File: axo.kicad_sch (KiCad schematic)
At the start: 55 parts, among them Q1 MMBT3904, Q2 MMBT3904, Q3 MMBT3904, Q4 MMBT3904, U1 74HC00, U2 74HC86, U3 74HC02, U4 LM1117-5.0

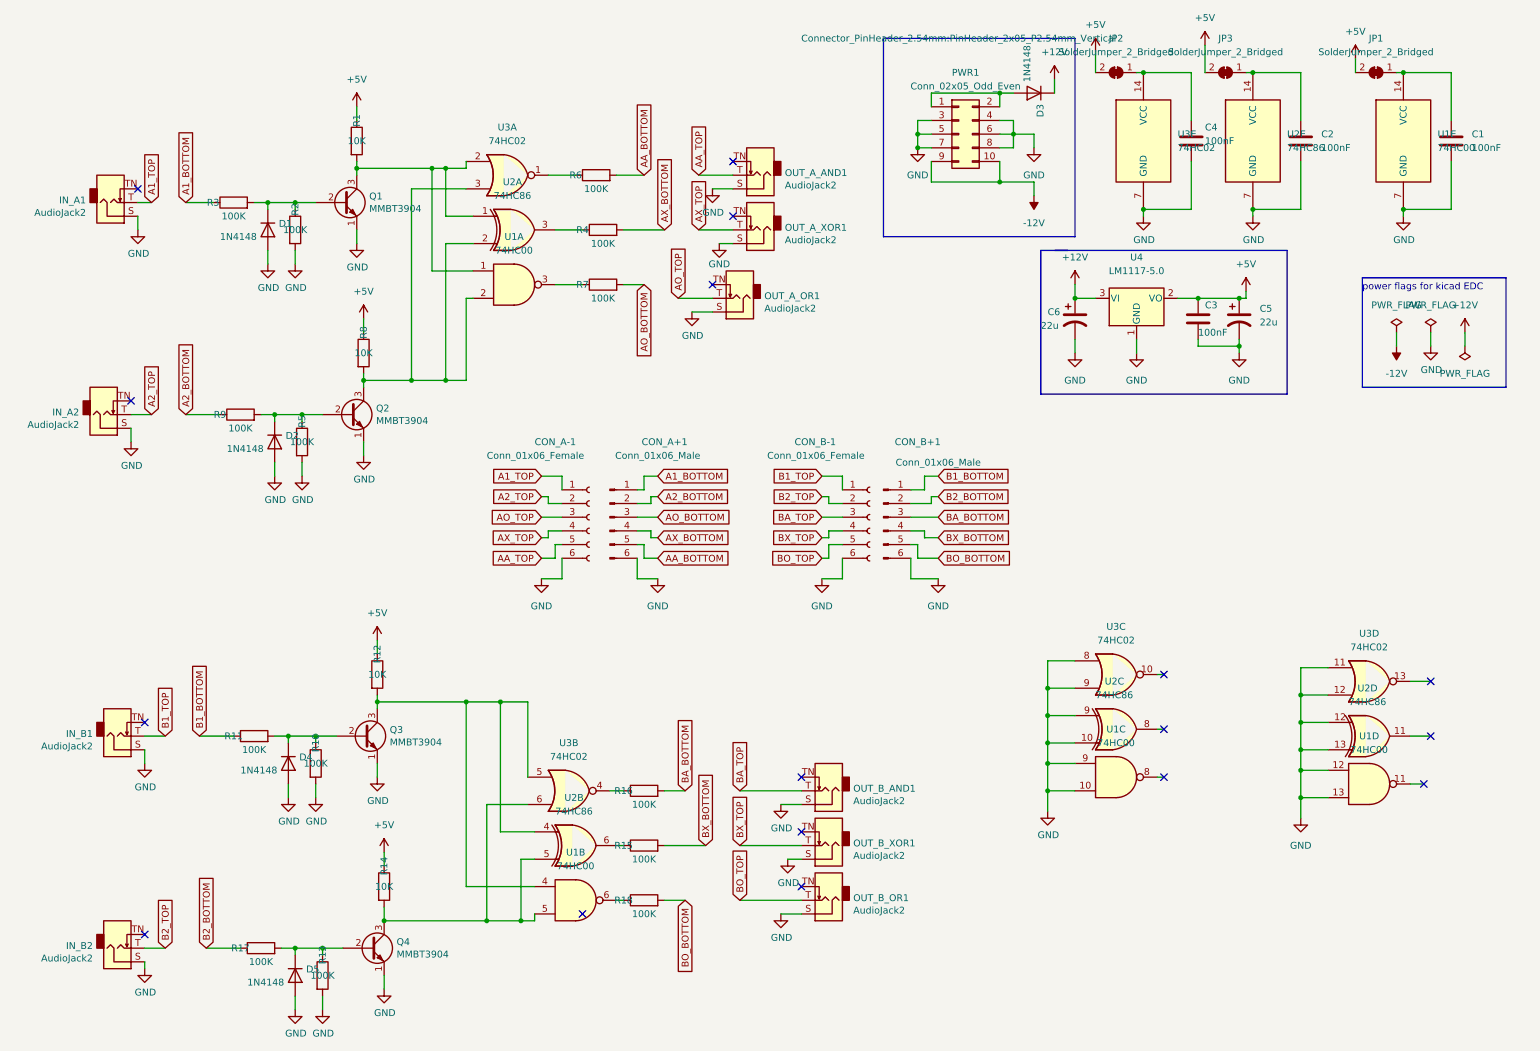
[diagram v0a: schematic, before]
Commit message: replace xor by nand/nor logic
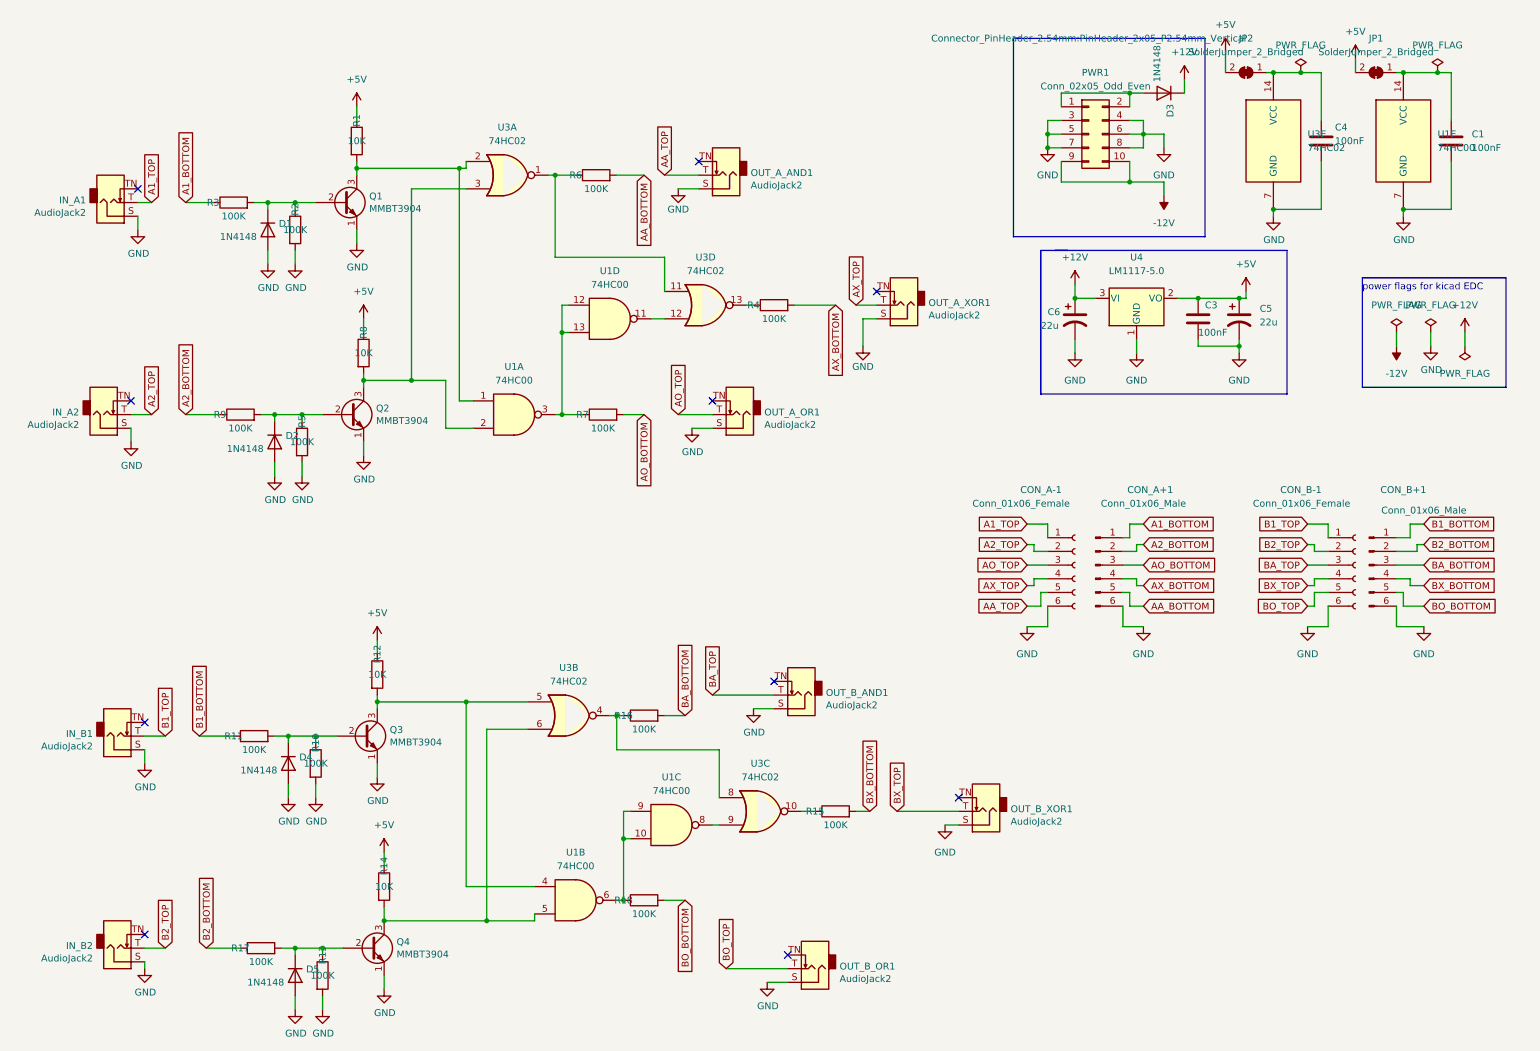
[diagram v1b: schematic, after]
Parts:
- removed C2: 100nF, Capacitor_SMD:C_0805_2012Metric, symbol Device:C
- removed JP3: SolderJumper_2_Bridged, Jumper:SolderJumper-2_P1.3mm_Bridged_Pad1.0x1.5mm, symbol Jumper:SolderJumper_2_Bridged
- removed U2: 74HC86, Package_SO:SOIC-14_3.9x8.7mm_P1.27mm, symbol 74xx:74HC86
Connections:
- net GND: no longer U1.10, U1.12, U1.13, U1.9, U3.11, U3.12, U3.8, U3.9
- net at R18.1, U1.6: now also U1.10, U1.9
- net at R15.1: now also U3.10
- net at R16.1, U3.4: now also U3.8
- net at R4.1: now also U3.13
- net at U1.11: now also U3.12
- net at R7.1, U1.3: now also U1.12, U1.13
- net at R6.1, U3.1: now also U3.11
- net at U1.8: now also U3.9
- no-connect marks 17 -> 10
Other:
- moved on the sheet: C4, CON_A+1, CON_A-1, CON_B+1, CON_B-1, D3, JP2, OUT_A_AND1, OUT_A_OR1, OUT_A_XOR1, OUT_B_AND1, OUT_B_OR1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

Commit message: add readme
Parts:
- removed Q1, Q2, Q3, Q4: MMBT3904, Package_TO_SOT_SMD:SOT-23, symbol Device:Q_NPN_EBC
- added Q1, Q2, Q3, Q4: MMBT3904, Package_TO_SOT_SMD:SOT-23, symbol Transistor_BJT:MMBT3904
- CON_A+1, CON_B+1: value Conn_01x06_Male -> Conn_01x06_Pin; symbol Connector:Conn_01x06_Male -> Connector:Conn_01x06_Pin
- CON_A-1, CON_B-1: value Conn_01x06_Female -> Conn_01x06_Socket; symbol Connector:Conn_01x06_Female -> Connector:Conn_01x06_Socket
- U4: value LM1117-5.0 -> LM1117MP-5.0; symbol Regulator_Linear:LM1117-5.0 -> Regulator_Linear:LM1117MP-5.0; LCSC C473812 -> C6187
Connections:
- net GND: now also Q1.2 (E), Q2.2 (E), Q3.2 (E), Q4.2 (E); no longer CON_A-1.6 (Pin_6), CON_B-1.6 (Pin_6), IN_A1.S, IN_A2.S, IN_B1.S, IN_B2.S, OUT_A_AND1.S, OUT_A_OR1.S, OUT_A_XOR1.S, OUT_B_AND1.S, OUT_B_OR1.S, OUT_B_XOR1.S
- net at R12.2, U1.4, U3.5: now also Q3.3 (C)
- net at R14.2, U1.5, U3.6: now also Q4.3 (C)
- net at D2.1 (K), R5.1, R9.2: now also Q2.1 (B)
- net at R8.2, U1.2, U3.3: now also Q2.3 (C)
- net at D1.1 (K), R2.1, R3.2: now also Q1.1 (B)
- net at D5.1 (K), R13.1, R17.2: now also Q4.1 (B)
- net at R1.2, U1.1, U3.2: now also Q1.3 (C)
- net at D4.1 (K), R10.1, R11.2: now also Q3.1 (B)
- new net GND2: CON_A-1.6 (Pin_6), CON_B-1.6 (Pin_6), IN_A1.S, IN_A2.S, IN_B1.S, IN_B2.S, OUT_A_AND1.S, OUT_A_OR1.S, OUT_A_XOR1.S, OUT_B_AND1.S, OUT_B_OR1.S, OUT_B_XOR1.S
